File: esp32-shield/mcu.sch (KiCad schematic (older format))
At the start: 29 parts, among them J11 DNP, J5 Conn_01x14_Female, J6 Conn_01x14_Female, Q3 S8050, Q4 S8050, SW1 SKRKAEE020, U13 ESP32-WROOM32, U14 W25Q32JVSS, U5 CH340C, U6 AMS1117-3.3, Y1 12MHZ

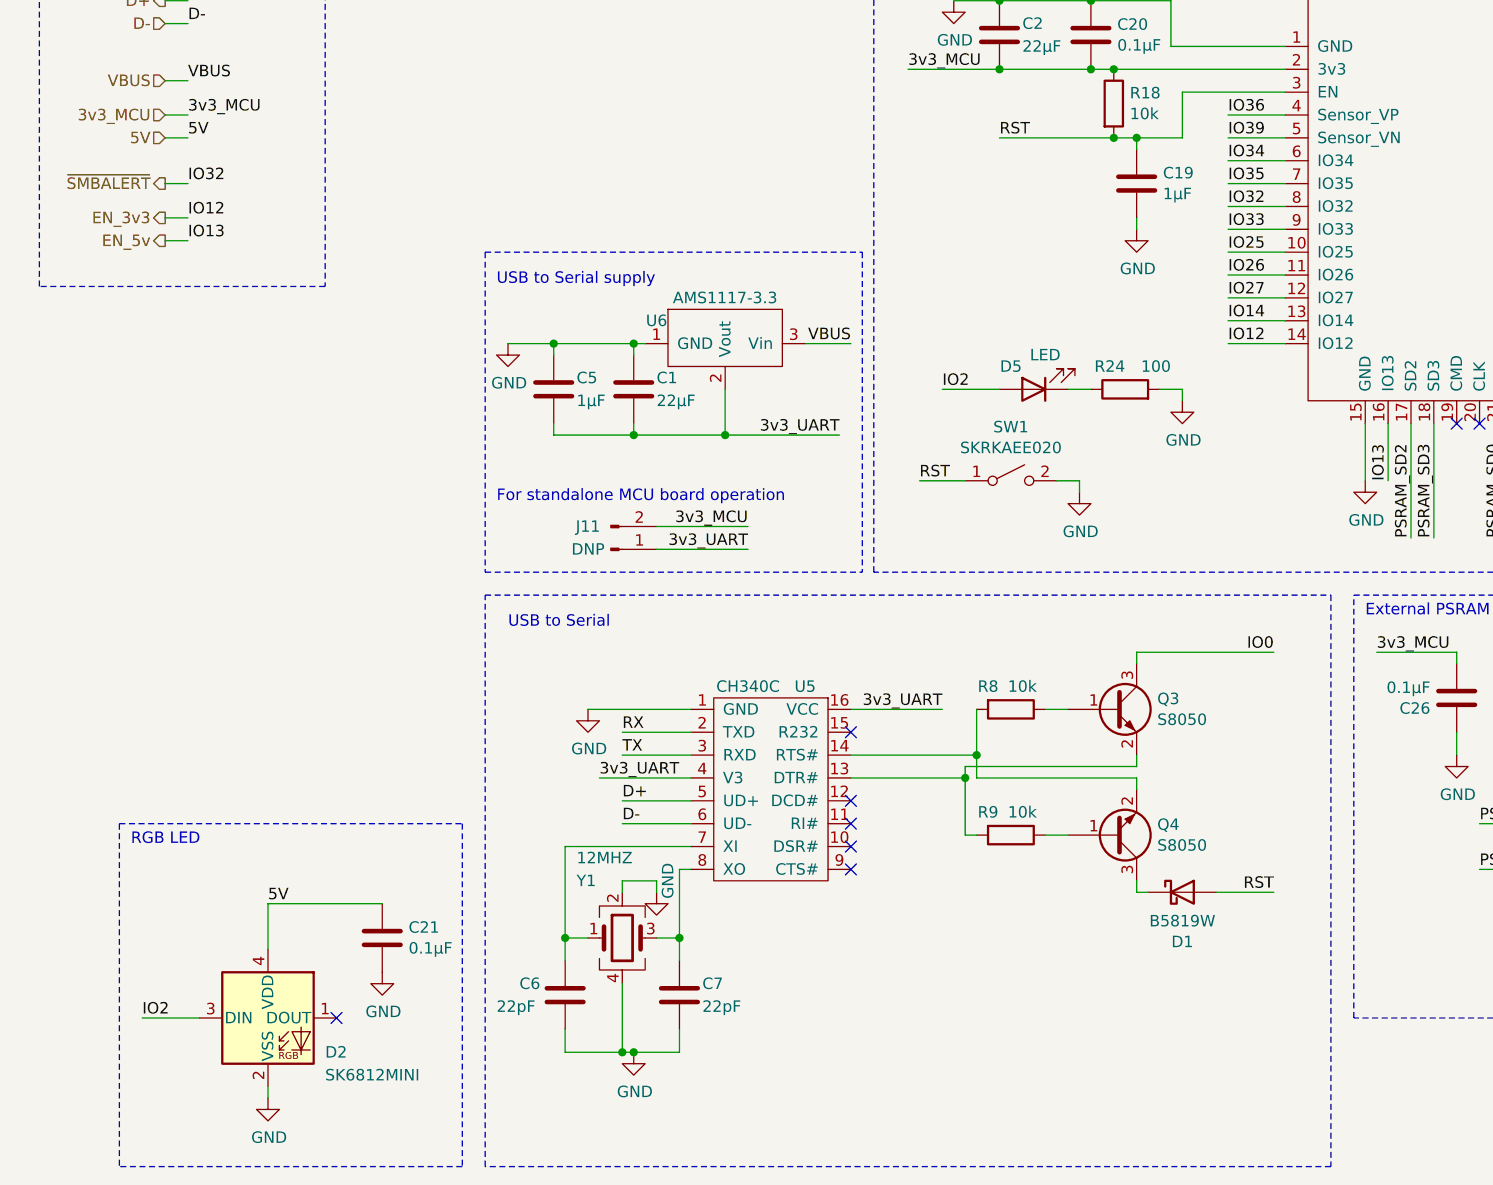
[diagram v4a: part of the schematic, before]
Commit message: swapped led for WS2812 footprint with logic level shifter
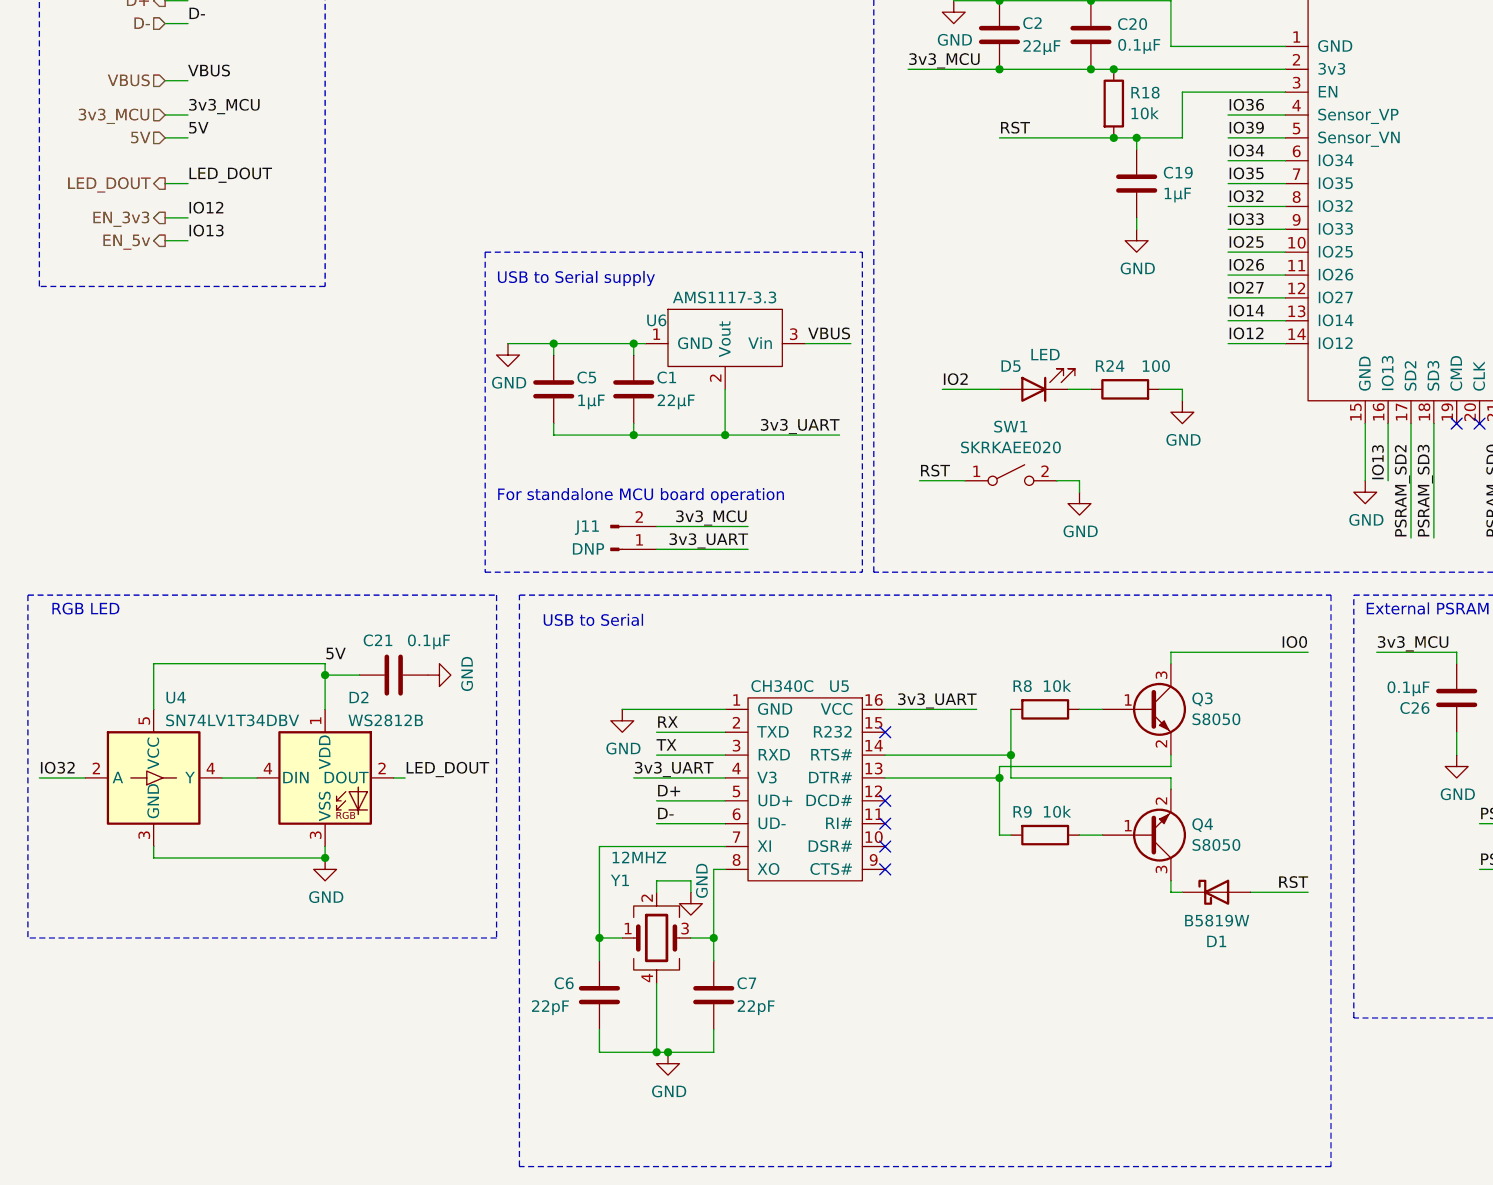
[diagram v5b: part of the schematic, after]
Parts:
- removed D2: SK6812MINI, LED_SMD:LED_SK6812MINI_PLCC4_3.5x3.5mm_P1.75mm, symbol LED:SK6812MINI
- added D2: WS2812B, LED_SMD:LED_WS2812B_PLCC4_5.0x5.0mm_P3.2mm, symbol LED:WS2812B
- added U4: SN74LV1T34DBV, Package_TO_SOT_SMD:SOT-23-5, symbol Logic_LevelTranslator:SN74LV1T34DBV
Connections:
- net 5V: now also D2.1 (VDD), U4.5 (VCC)
- net GND: now also D2.3 (VSS), U4.3 (GND)
- net ~SMBALERT renamed IO32
- net IO32: now also U4.2 (A)
- new net: D2.4 (DIN), U4.4 (Y)
- new net LED_DOUT: D2.2 (DOUT)
- no-connect marks 9 -> 8
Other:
- moved on the sheet: C21, C6, C7, D1, Q3, Q4, R8, R9, U5, Y1

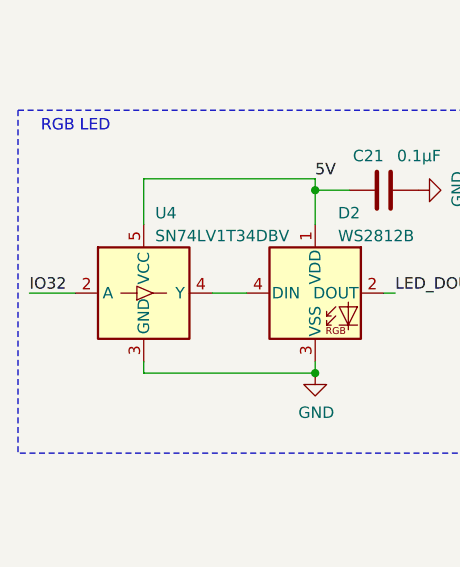
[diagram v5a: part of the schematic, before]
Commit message: RGB led on right side and using pin 2
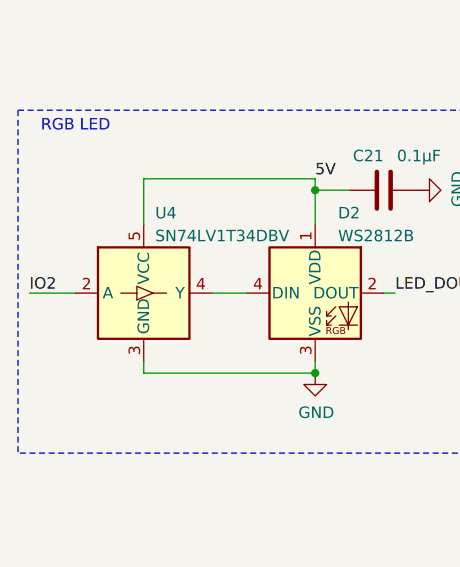
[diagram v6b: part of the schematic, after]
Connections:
- net IO2: now also U4.2 (A)
- net IO32: no longer U4.2 (A)
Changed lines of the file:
@@
 	7300 3450 7300 3200
 Text Label 600  4750 0    50   ~ 0
-IO32
+IO2
 Wire Wire Line
 	1850 5050 1850 5100

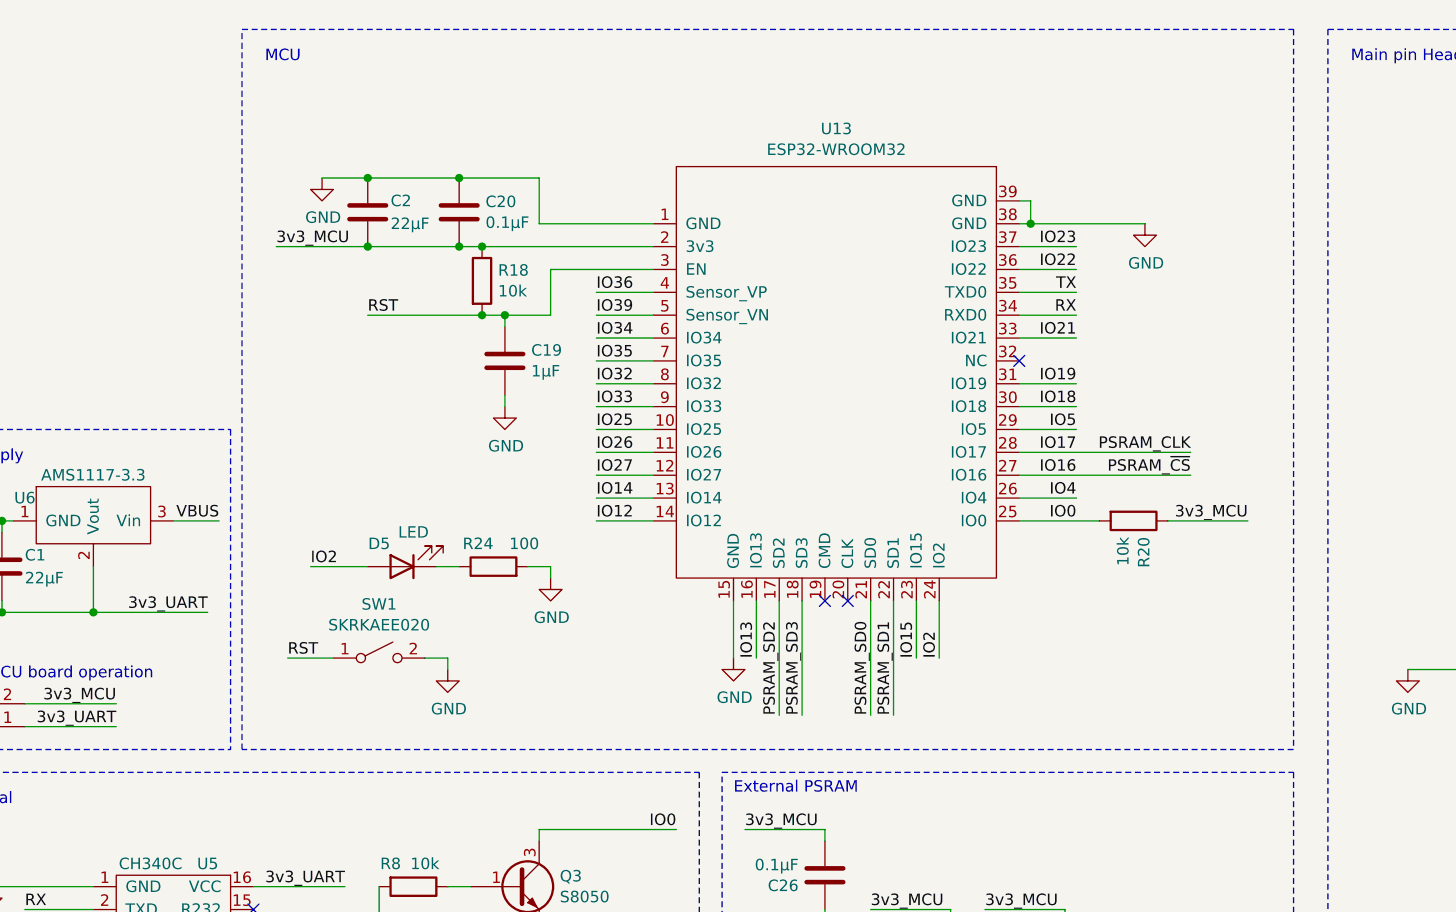
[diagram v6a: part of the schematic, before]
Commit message: added another 22µ cap to 3v3mcu rail
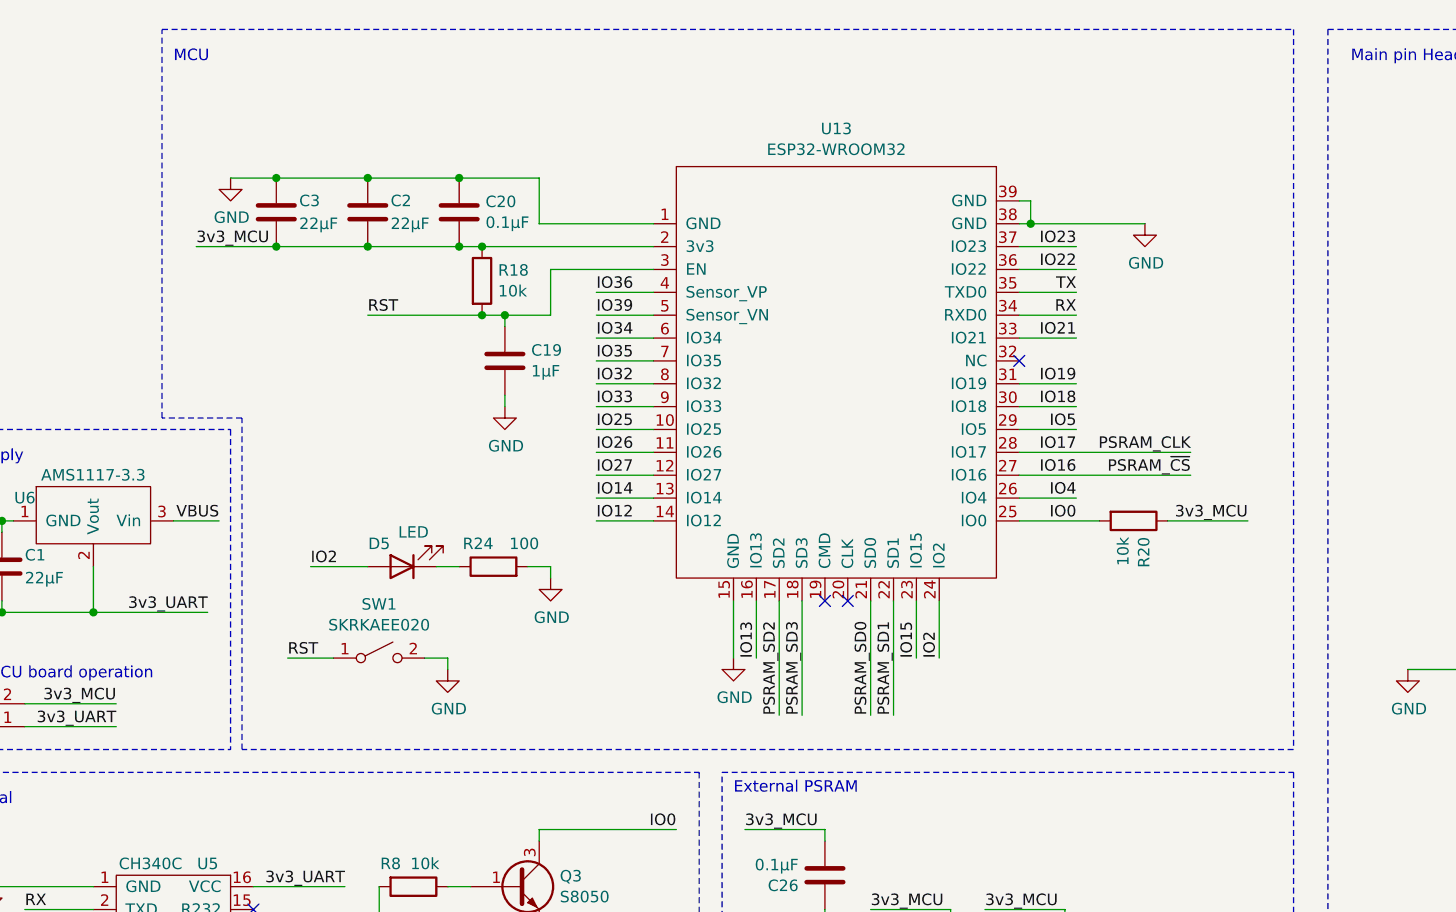
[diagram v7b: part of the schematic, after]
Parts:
- added C3: 22µF, Capacitor_SMD:C_0805_2012Metric, symbol Device:C
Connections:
- net 3v3_MCU: now also C3.2
- net GND: now also C3.1
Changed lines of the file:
@@
 L power:GND #PWR0116
 U 1 1 5F82BD5E
-P 4600 1350
-F 0 "#PWR0116" H 4600 1100 50  0001 C CNN
-F 1 "GND" H 4605 1177 50  0000 C CNN
-F 2 "" H 4600 1350 50  0001 C CNN
-F 3 "" H 4600 1350 50  0001 C CNN
-	1    4600 1350
+P 4200 1350
+F 0 "#PWR0116" H 4200 1100 50  0001 C CNN
+F 1 "GND" H 4205 1177 50  0000 C CNN
+F 2 "" H 4200 1350 50  0001 C CNN
+F 3 "" H 4200 1350 50  0001 C CNN
+	1    4200 1350
 	1    0    0    -1
 $EndComp
@@
 	9000 5800 11000 5800
 Wire Notes Line
-	4250 700  8850 700
-Wire Notes Line
 	8850 700  8850 3850
 Wire Notes Line
 	8850 3850 4250 3850
-Text Notes 4350 850  0    50   ~ 0
+Text Notes 3950 850  0    50   ~ 0
 MCU
-Text Label 4400 1650 0    50   ~ 0
+Text Label 4050 1650 0    50   ~ 0
 3v3_MCU
 Wire Wire Line
@@
 Text Label 4450 3450 0    50   ~ 0
 RST
-Wire Notes Line
-	4250 3850 4250 700
 Wire Wire Line
 	5300 1950 5400 1950
@@
 Wire Wire Line
 	3200 3250 3600 3250
-Connection ~ 4800 1350
 Wire Wire Line
 	4800 1350 5200 1350
@@
 	4400 1650 4800 1650
 Wire Wire Line
-	4600 1350 4800 1350
+	4200 1350 4400 1350
 $Comp
 L Device:C C?
@@
 Wire Notes Line
 	550  3950 2600 3950
+$Comp
+L Device:C C?
+U 1 1 60BF269B
+P 4400 1500
+AR Path="/5F63B107/60BF269B" Ref="C?"  Part="1"
+AR Path="/5F63A193/60BF269B" Ref="C3"  Part="1"
+F 0 "C3" H 4500 1550 50  0000 L CNN
+F 1 "22µF" H 4500 1450 50  0000 L CNN
+F 2 "Capacitor_SMD:C_0805_2012Metric" H 4438 1350 50  0001 C CNN
+F 3 "~" H 4400 1500 50  0001 C CNN
+F 4 "C45783" H 4400 1500 50  0001 C CNN "LCSC"
+	1    4400 1500
+	1    0    0    -1
+$EndComp
+Wire Notes Line
+	4250 3850 4250 2400
+Wire Notes Line
+	4250 2400 3900 2400
+Wire Notes Line
+	3900 2400 3900 700
+Wire Notes Line
+	3900 700  8850 700
+Wire Wire Line
+	4400 1650 4050 1650
+Connection ~ 4400 1650
+Wire Wire Line
+	4400 1350 4800 1350
+Connection ~ 4400 1350
+Connection ~ 4800 1350
 $EndSCHEMATC
